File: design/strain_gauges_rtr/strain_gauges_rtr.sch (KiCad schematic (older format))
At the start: 16 parts, among them J1 Conn_01x03, J2 Conn_01x03, J3 Conn_01x08, P1 CONN_01X02, Q1 2N3096, U1 TL780-15, U2 LT1460-10

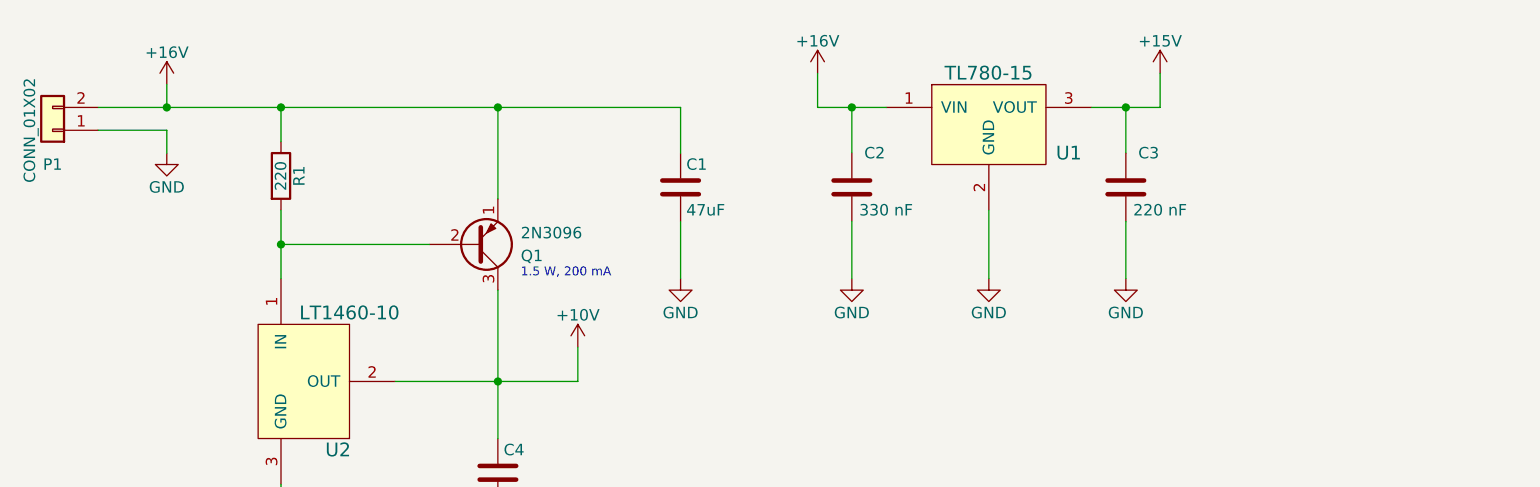
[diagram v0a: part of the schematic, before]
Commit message: Add fuses to both strain gauge circuits.
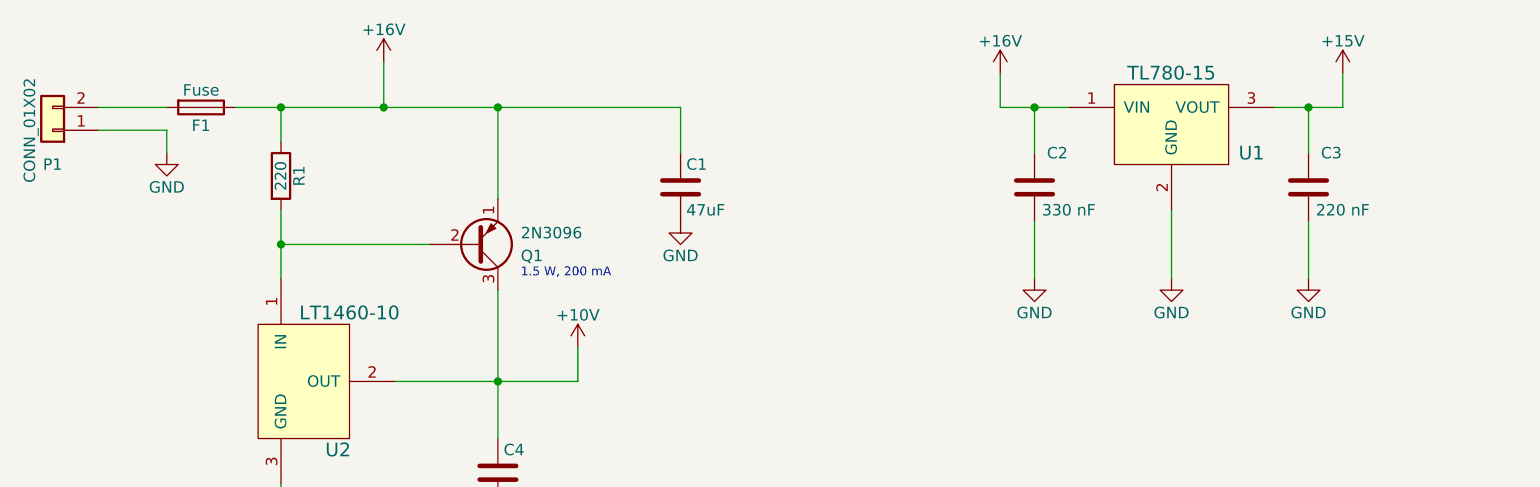
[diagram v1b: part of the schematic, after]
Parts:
- added F1: Fuse, Fuse:Fuse_1206_3216Metric_Pad1.24x1.80mm_HandSolder, symbol Fuse
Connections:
- net +16V: now also F1.1; no longer P1.2 (Pin_2)
- new net: F1.2, P1.2 (Pin_2)
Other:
- moved on the sheet: C2, C3, U1
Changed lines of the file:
@@
 L GND #PWR02
 U 1 1 5ACADCBE
-P 4050 2000
-F 0 "#PWR02" H 4050 1750 50  0001 C CNN
-F 1 "GND" H 4050 1850 50  0000 C CNN
-F 2 "" H 4050 2000 50  0000 C CNN
-F 3 "" H 4050 2000 50  0000 C CNN
-	1    4050 2000
+P 4050 1750
+F 0 "#PWR02" H 4050 1500 50  0001 C CNN
+F 1 "GND" H 4050 1600 50  0000 C CNN
+F 2 "" H 4050 1750 50  0000 C CNN
+F 3 "" H 4050 1750 50  0000 C CNN
+	1    4050 1750
 	1    0    0    -1
 $EndComp
@@
 L +16V #PWR05
 U 1 1 5ACADCD7
-P 1800 1150
-F 0 "#PWR05" H 1800 1000 50  0001 C CNN
-F 1 "+16V" H 1800 1290 50  0000 C CNN
-F 2 "" H 1800 1150 50  0000 C CNN
-F 3 "" H 1800 1150 50  0000 C CNN
-	1    1800 1150
+P 2750 1050
+F 0 "#PWR05" H 2750 900 50  0001 C CNN
+F 1 "+16V" H 2750 1190 50  0000 C CNN
+F 2 "" H 2750 1050 50  0000 C CNN
+F 3 "" H 2750 1050 50  0000 C CNN
+	1    2750 1050
 	1    0    0    -1
 $EndComp
@@
 Text Notes 3350 2000 0    39   ~ 0
 1.5 W, 200 mA
-Wire Wire Line
-	1500 1250 4050 1250
-Wire Wire Line
-	1800 1350 1500 1350
-Wire Wire Line
-	1800 1450 1800 1350
-Wire Wire Line
-	3600 2450 3600 2300
-Wire Wire Line
-	2300 1250 2300 1400
-Wire Wire Line
-	2950 1850 2300 1850
-Connection ~ 2300 1850
-Wire Wire Line
-	3250 2050 3250 2700
-Wire Wire Line
-	2800 2450 3600 2450
-Connection ~ 3250 2450
-Connection ~ 2300 1250
-Wire Wire Line
-	1800 1250 1800 1150
-Connection ~ 1800 1250
-Wire Wire Line
-	2300 1700 2300 2000
-Connection ~ 3250 1250
-Wire Wire Line
-	4050 1750 4050 2000
-Wire Wire Line
-	4050 1250 4050 1450
-Wire Wire Line
-	2300 2900 2300 3100
-Wire Wire Line
-	3250 1250 3250 1650
-Wire Wire Line
-	2300 3100 3250 3100
-Wire Wire Line
-	2750 3200 2750 3100
-Connection ~ 2750 3100
-Wire Wire Line
-	3250 3100 3250 3000
 $Comp
 L +16V #PWR06
 U 1 1 5ACAE219
-P 4650 1100
-F 0 "#PWR06" H 4650 950 50  0001 C CNN
-F 1 "+16V" H 4650 1240 50  0000 C CNN
-F 2 "" H 4650 1100 50  0000 C CNN
-F 3 "" H 4650 1100 50  0000 C CNN
-	1    4650 1100
+P 5450 1100
+F 0 "#PWR06" H 5450 950 50  0001 C CNN
+F 1 "+16V" H 5450 1240 50  0000 C CNN
+F 2 "" H 5450 1100 50  0000 C CNN
+F 3 "" H 5450 1100 50  0000 C CNN
+	1    5450 1100
 	1    0    0    -1
 $EndComp
@@
 L GND #PWR07
 U 1 1 5ACAE21F
-P 5400 2000
-F 0 "#PWR07" H 5400 1750 50  0001 C CNN
-F 1 "GND" H 5400 1850 50  0000 C CNN
-F 2 "" H 5400 2000 50  0001 C CNN
-F 3 "" H 5400 2000 50  0001 C CNN
-	1    5400 2000
+P 6200 2000
+F 0 "#PWR07" H 6200 1750 50  0001 C CNN
+F 1 "GND" H 6200 1850 50  0000 C CNN
+F 2 "" H 6200 2000 50  0001 C CNN
+F 3 "" H 6200 2000 50  0001 C CNN
+	1    6200 2000
 	1    0    0    -1
 $EndComp
@@
 L C C2
 U 1 1 5ACAE225
-P 4800 1600
-F 0 "C2" H 4900 1750 50  0000 C CNN
-F 1 "330 nF" H 4950 1500 50  0000 C CNN
-F 2 "Capacitors_SMD:C_0805_HandSoldering" H 4800 1600 50  0001 C CNN
-F 3 "" H 4800 1600 50  0001 C CNN
-	1    4800 1600
+P 5600 1600
+F 0 "C2" H 5700 1750 50  0000 C CNN
+F 1 "330 nF" H 5750 1500 50  0000 C CNN
+F 2 "Capacitors_SMD:C_0805_HandSoldering" H 5600 1600 50  0001 C CNN
+F 3 "" H 5600 1600 50  0001 C CNN
+	1    5600 1600
 	1    0    0    -1
 $EndComp
@@
 L C C3
 U 1 1 5ACAE22C
-P 6000 1600
-F 0 "C3" H 6100 1750 50  0000 C CNN
-F 1 "220 nF" H 6150 1500 50  0000 C CNN
-F 2 "Capacitors_SMD:C_0805_HandSoldering" H 6000 1600 50  0001 C CNN
-F 3 "" H 6000 1600 50  0001 C CNN
-	1    6000 1600
+P 6800 1600
+F 0 "C3" H 6900 1750 50  0000 C CNN
+F 1 "220 nF" H 6950 1500 50  0000 C CNN
+F 2 "Capacitors_SMD:C_0805_HandSoldering" H 6800 1600 50  0001 C CNN
+F 3 "" H 6800 1600 50  0001 C CNN
+	1    6800 1600
 	1    0    0    -1
 $EndComp
@@
 L GND #PWR08
 U 1 1 5ACAE233
-P 6000 2000
-F 0 "#PWR08" H 6000 1750 50  0001 C CNN
-F 1 "GND" H 6000 1850 50  0000 C CNN
-F 2 "" H 6000 2000 50  0001 C CNN
-F 3 "" H 6000 2000 50  0001 C CNN
-	1    6000 2000
+P 6800 2000
+F 0 "#PWR08" H 6800 1750 50  0001 C CNN
+F 1 "GND" H 6800 1850 50  0000 C CNN
+F 2 "" H 6800 2000 50  0001 C CNN
+F 3 "" H 6800 2000 50  0001 C CNN
+	1    6800 2000
 	1    0    0    -1
 $EndComp
@@
 L GND #PWR09
 U 1 1 5ACAE239
-P 4800 2000
-F 0 "#PWR09" H 4800 1750 50  0001 C CNN
-F 1 "GND" H 4800 1850 50  0000 C CNN
-F 2 "" H 4800 2000 50  0001 C CNN
-F 3 "" H 4800 2000 50  0001 C CNN
-	1    4800 2000
+P 5600 2000
+F 0 "#PWR09" H 5600 1750 50  0001 C CNN
+F 1 "GND" H 5600 1850 50  0000 C CNN
+F 2 "" H 5600 2000 50  0001 C CNN
+F 3 "" H 5600 2000 50  0001 C CNN
+	1    5600 2000
 	1    0    0    -1
 $EndComp
@@
 L TL780-15 U1
 U 1 1 5ACAE23F
-P 5300 1000
-F 0 "U1" H 5750 550 60  0000 C CNN
-F 1 "TL780-15" H 5400 900 60  0000 C CNN
-F 2 "TO_SOT_Packages_THT:TO-220-3_Vertical" H 5300 1000 60  0001 C CNN
-F 3 "" H 5300 1000 60  0001 C CNN
-	1    5300 1000
+P 6100 1000
+F 0 "U1" H 6550 550 60  0000 C CNN
+F 1 "TL780-15" H 6200 900 60  0000 C CNN
+F 2 "TO_SOT_Packages_THT:TO-220-3_Vertical" H 6100 1000 60  0001 C CNN
+F 3 "" H 6100 1000 60  0001 C CNN
+	1    6100 1000
 	1    0    0    -1
 $EndComp
@@
 L +15V #PWR010
 U 1 1 5ACAE246
-P 6150 1100
-F 0 "#PWR010" H 6150 950 50  0001 C CNN
-F 1 "+15V" H 6150 1240 50  0000 C CNN
-F 2 "" H 6150 1100 50  0000 C CNN
-F 3 "" H 6150 1100 50  0000 C CNN
-	1    6150 1100
-	1    0    0    -1
-$EndComp
-Wire Wire Line
-	4650 1100 4650 1250
-Wire Wire Line
-	4650 1250 4950 1250
-Wire Wire Line
-	6150 1250 6150 1100
-Wire Wire Line
-	5850 1250 6150 1250
-Wire Wire Line
-	5400 1700 5400 2000
-Wire Wire Line
-	6000 1750 6000 2000
-Wire Wire Line
-	4800 1750 4800 2000
-Wire Wire Line
-	4800 1250 4800 1450
-Connection ~ 4800 1250
-Wire Wire Line
-	6000 1250 6000 1450
-Connection ~ 6000 1250
+P 6950 1100
+F 0 "#PWR010" H 6950 950 50  0001 C CNN
+F 1 "+15V" H 6950 1240 50  0000 C CNN
+F 2 "" H 6950 1100 50  0000 C CNN
+F 3 "" H 6950 1100 50  0000 C CNN
+	1    6950 1100
+	1    0    0    -1
+$EndComp
 $Comp
 L Conn_01x03 J1
@@
 Text Label 8950 3800 2    60   ~ 0
 PRESSURE_2
-Wire Wire Line
-	8950 3300 9600 3300
-Wire Wire Line
-	8950 3400 9600 3400
-Wire Wire Line
-	8950 3500 9600 3500
-Wire Wire Line
-	8950 3600 9600 3600
-Wire Wire Line
-	8950 3700 9600 3700
-Wire Wire Line
-	8950 3800 9600 3800
-Wire Wire Line
-	9350 1200 9350 1400
-Wire Wire Line
-	9350 1400 9050 1400
-Wire Wire Line
-	9050 1500 9500 1500
-Wire Wire Line
-	9500 1500 9500 1250
-Wire Wire Line
-	9500 1250 9700 1250
-Wire Wire Line
-	9200 1600 9050 1600
-Wire Wire Line
-	9350 2050 9350 2250
-Wire Wire Line
-	9350 2250 9050 2250
-Wire Wire Line
-	9050 2350 9500 2350
-Wire Wire Line
-	9500 2350 9500 2100
-Wire Wire Line
-	9500 2100 9700 2100
-Wire Wire Line
-	9200 2450 9050 2450
-Wire Wire Line
-	9050 5250 9050 5300
-Wire Wire Line
-	9050 5700 9050 5600
-Wire Wire Line
-	8550 5250 8550 5300
-Wire Wire Line
-	8550 5700 8550 5600
-Wire Wire Line
-	9050 5300 9300 5300
-Wire Wire Line
-	8550 5300 8750 5300
-Wire Wire Line
-	8750 5300 8750 3900
-Wire Wire Line
-	8750 3900 9600 3900
-Wire Wire Line
-	9300 5300 9300 4000
-Wire Wire Line
-	9300 4000 9600 4000
 $Sheet
 S 1300 4000 1950 1250
@@
 Text Label 6700 4300 0    60   ~ 0
 STRAIN_OUT_2
-Wire Wire Line
-	3250 4300 3500 4300
-Wire Wire Line
-	6350 4300 6700 4300
 Text Label 3500 5950 0    60   ~ 0
 STRAIN_OUT_3
-Wire Wire Line
-	3500 5950 3250 5950
 Text Label 6700 5950 0    60   ~ 0
 STRAIN_OUT_4
 Wire Wire Line
+	2100 1250 4050 1250
+Wire Wire Line
+	1800 1350 1500 1350
+Wire Wire Line
+	1800 1450 1800 1350
+Wire Wire Line
+	2300 1250 2300 1400
+Wire Wire Line
+	2950 1850 2300 1850
+Connection ~ 2300 1850
+Wire Wire Line
+	3250 2050 3250 2700
+Wire Wire Line
+	2800 2450 3600 2450
+Connection ~ 3250 2450
+Connection ~ 2300 1250
+Wire Wire Line
+	2300 1700 2300 2000
+Connection ~ 3250 1250
+Wire Wire Line
+	4050 1250 4050 1450
+Wire Wire Line
+	2300 2900 2300 3100
+Wire Wire Line
+	3250 1250 3250 1650
+Wire Wire Line
+	2300 3100 3250 3100
+Wire Wire Line
+	2750 3200 2750 3100
+Connection ~ 2750 3100
+Wire Wire Line
+	3250 3100 3250 3000
+Wire Wire Line
+	5450 1100 5450 1250
+Wire Wire Line
+	5450 1250 5750 1250
+Wire Wire Line
+	6950 1250 6950 1100
+Wire Wire Line
+	6650 1250 6950 1250
+Wire Wire Line
+	6200 1700 6200 2000
+Wire Wire Line
+	6800 1750 6800 2000
+Wire Wire Line
+	5600 1750 5600 2000
+Wire Wire Line
+	5600 1250 5600 1450
+Connection ~ 5600 1250
+Wire Wire Line
+	6800 1250 6800 1450
+Connection ~ 6800 1250
+Wire Wire Line
+	8950 3300 9600 3300
+Wire Wire Line
+	8950 3400 9600 3400
+Wire Wire Line
+	8950 3500 9600 3500
+Wire Wire Line
+	8950 3600 9600 3600
+Wire Wire Line
+	8950 3700 9600 3700
+Wire Wire Line
+	8950 3800 9600 3800
+Wire Wire Line
+	9350 1200 9350 1400
+Wire Wire Line
+	9350 1400 9050 1400
+Wire Wire Line
+	9050 1500 9500 1500
+Wire Wire Line
+	9500 1500 9500 1250
+Wire Wire Line
+	9500 1250 9700 1250
+Wire Wire Line
+	9200 1600 9050 1600
+Wire Wire Line
+	9350 2050 9350 2250
+Wire Wire Line
+	9350 2250 9050 2250
+Wire Wire Line
+	9050 2350 9500 2350
+Wire Wire Line
+	9500 2350 9500 2100
+Wire Wire Line
+	9500 2100 9700 2100
+Wire Wire Line
+	9200 2450 9050 2450
+Wire Wire Line
+	9050 5250 9050 5300
+Wire Wire Line
+	9050 5700 9050 5600
+Wire Wire Line
+	8550 5250 8550 5300
+Wire Wire Line
+	8550 5700 8550 5600
+Wire Wire Line
+	9050 5300 9300 5300
+Wire Wire Line
+	8550 5300 8750 5300
+Wire Wire Line
+	8750 5300 8750 3900
+Wire Wire Line
+	8750 3900 9600 3900
+Wire Wire Line
+	9300 5300 9300 4000
+Wire Wire Line
+	9300 4000 9600 4000
+Wire Wire Line
+	3250 4300 3500 4300
+Wire Wire Line
+	6350 4300 6700 4300
+Wire Wire Line
+	3500 5950 3250 5950
+Wire Wire Line
 	6700 5950 6350 5950
+Wire Wire Line
+	3600 2450 3600 2300
+Wire Wire Line
+	2750 1050 2750 1250
+Connection ~ 2750 1250
+$Comp
+L Fuse F1
+U 1 1 5ACB8796
+P 1950 1250
+F 0 "F1" V 2030 1250 50  0000 C CNN
+F 1 "Fuse" V 1875 1250 50  0000 C CNN
+F 2 "Fuse:Fuse_1206_3216Metric_Pad1.24x1.80mm_HandSolder" V 1880 1250 50  0001 C CNN
+F 3 "" H 1950 1250 50  0001 C CNN
+	1    1950 1250
+	0    1    1    0
+$EndComp
+Wire Wire Line
+	1800 1250 1500 1250
 $EndSCHEMATC

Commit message: Finish routing on INA826 board.
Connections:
- net PRESSURE_1: now also J3.3 (Pin_3); no longer J3.4 (Pin_4)
- net PRESSURE_2: now also J3.4 (Pin_4); no longer J3.3 (Pin_3)
- net STRAIN_OUT_1: now also J3.5 (Pin_5); no longer J3.8 (Pin_8)
- net STRAIN_OUT_2: now also J3.6 (Pin_6); no longer J3.7 (Pin_7)
- net STRAIN_OUT_3: now also J3.7 (Pin_7); no longer J3.6 (Pin_6)
- net STRAIN_OUT_4: now also J3.8 (Pin_8); no longer J3.5 (Pin_5)
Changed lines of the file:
@@
 Text Label 9200 2450 0    60   ~ 0
 PRESSURE_2
+Text Label 8950 3600 2    60   ~ 0
+STRAIN_OUT_1
+Text Label 8950 3500 2    60   ~ 0
+STRAIN_OUT_2
+Text Label 8950 3400 2    60   ~ 0
+STRAIN_OUT_3
 Text Label 8950 3300 2    60   ~ 0
-STRAIN_OUT_1
-Text Label 8950 3400 2    60   ~ 0
-STRAIN_OUT_2
-Text Label 8950 3500 2    60   ~ 0
-STRAIN_OUT_3
-Text Label 8950 3600 2    60   ~ 0
 STRAIN_OUT_4
+Text Label 8950 3800 2    60   ~ 0
+PRESSURE_1
 Text Label 8950 3700 2    60   ~ 0
-PRESSURE_1
-Text Label 8950 3800 2    60   ~ 0
 PRESSURE_2
 $Sheet
@@
 Text Label 3500 4300 0    60   ~ 0
 STRAIN_OUT_1
+Text Label 3500 5950 0    60   ~ 0
+STRAIN_OUT_2
 Text Label 6700 4300 0    60   ~ 0
-STRAIN_OUT_2
-Text Label 3500 5950 0    60   ~ 0
 STRAIN_OUT_3
 Text Label 6700 5950 0    60   ~ 0
